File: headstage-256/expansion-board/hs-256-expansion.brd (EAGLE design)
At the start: 34 x 28.2 mm, 16 parts, among them J2 PINHD-2X5_DF40-REC, J4 PINHD-2X5_DF40-REC, J5 PINHD-2X6, J6 PINHD-2X4

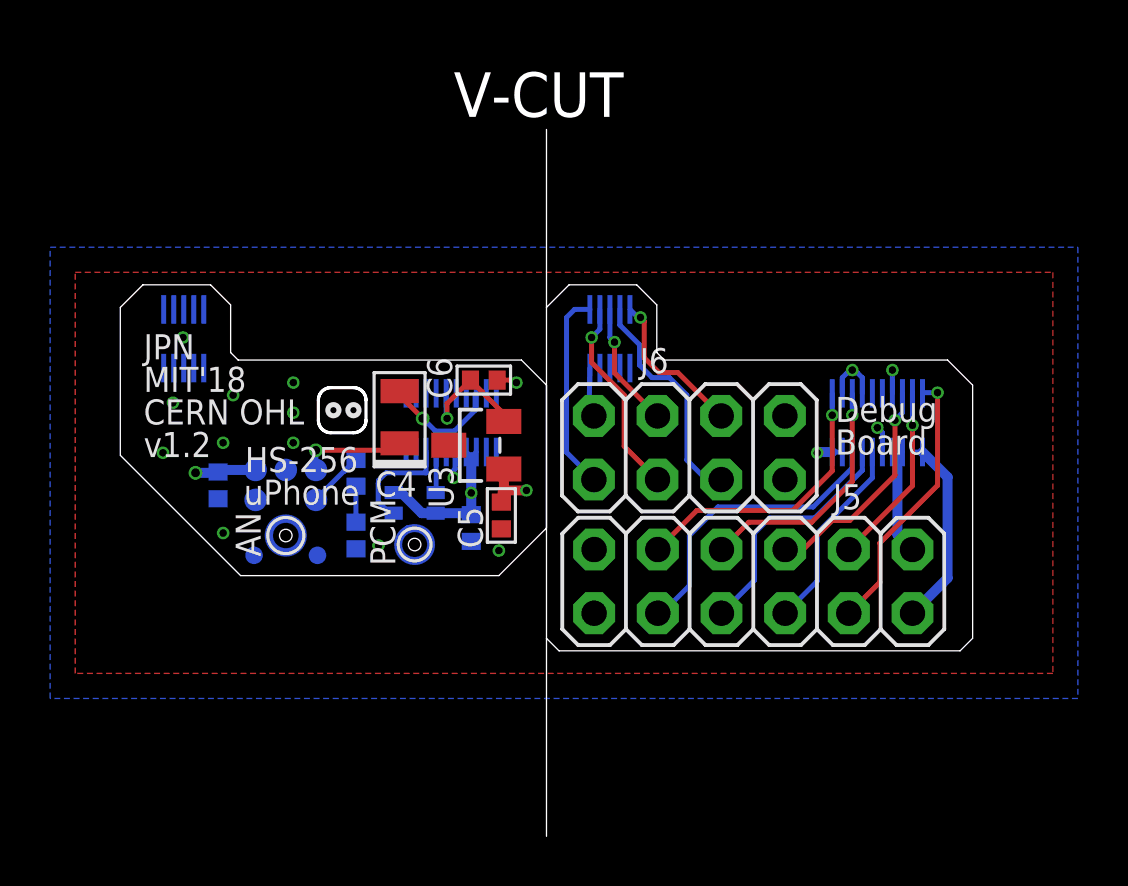
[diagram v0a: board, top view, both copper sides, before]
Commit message: Fix errors in headstage-256 expansion boards
- Headers were too close to receptacles in debug board
- Some components did not have values
- Added BOM to the google sheet based on this design
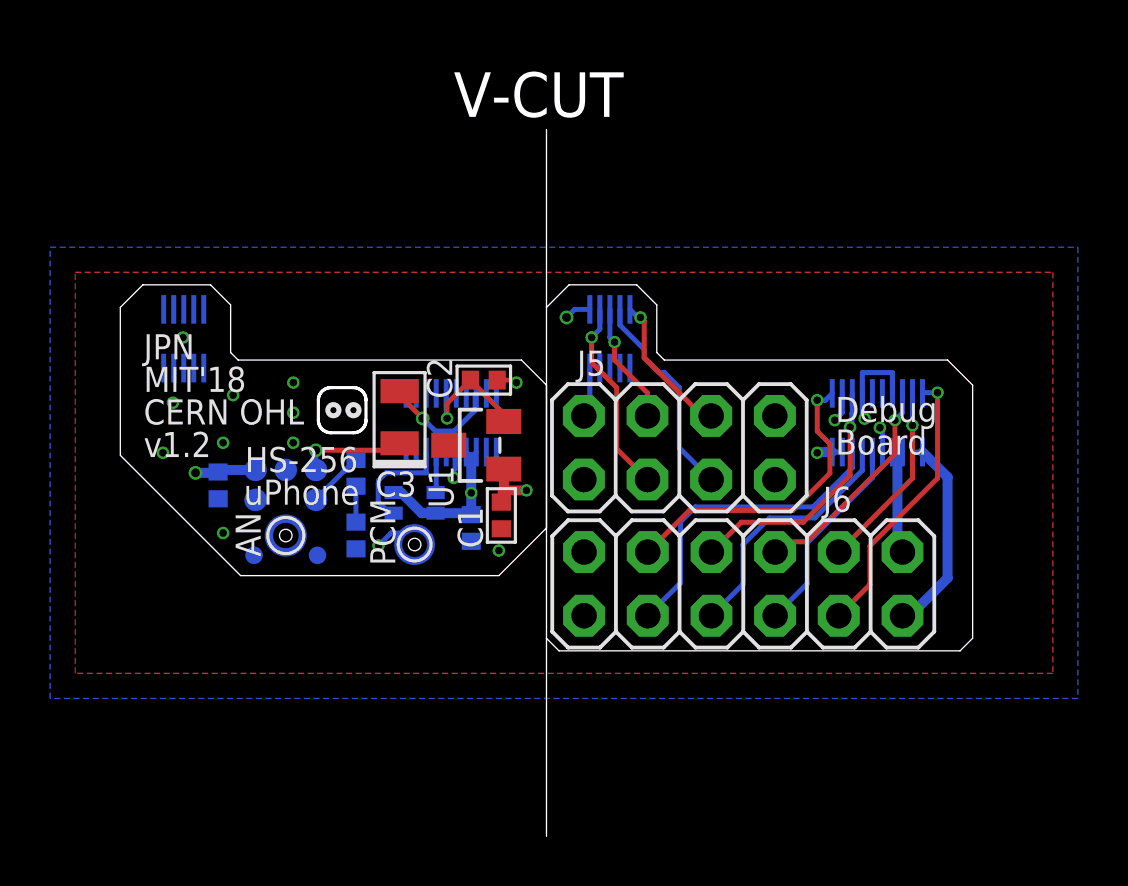
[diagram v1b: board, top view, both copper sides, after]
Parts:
- C3: value 1uF -> 10uF; device jonnew:0402 -> jonnew:0805-POL
- C4: value (none) -> 0.1uF; device jonnew:0805-POL -> jonnew:0402
- C5: value (none) -> 0.1uF
- C6: value 0.1uF -> 1uF
- J3: value (none) -> PINHD-2X5_DF40-REC; device jonnew:DF40-20REC -> jonnew:DF40-10REC
- J4: value PINHD-2X5_DF40-REC -> (none); device jonnew:DF40-10REC -> jonnew:DF40-20REC
- J5: value PINHD-2X6 -> PINHD-2X4; device jonnew:2X06-BIG -> jonnew:2X04-BIG
- J6: value PINHD-2X4 -> PINHD-2X6; device jonnew:2X04-BIG -> jonnew:2X06-BIG
- U1: value (none) -> REF3318; device jonnew:KNOWLES-SPH -> jonnew:SOT23
- U2: value (none) -> SPM0408LE5H-TB-6
- U3: value (none) -> SPH0641LU4H-1; device jonnew:SOT23 -> jonnew:KNOWLES-SPH
- moved C2 11.4 mm to (1.30, 1.70), flipped to the top, turned to 0 degrees
- moved C5 11.4 mm to (-9.30, -2.50), flipped to the bottom
- moved J3 11.2 mm to (6.33, 3.35)
- moved J4 11.2 mm to (17.0, 0.00)
- moved C6 8.03 mm to (-3.80, -4.50), flipped to the bottom, turned to 270 degrees
- moved J6 7.91 mm to (5.30, -7.70)
- moved J5 7.42 mm to (9.10, -1.00)
- moved C4 5.26 mm to (0.80, -4.20), flipped to the bottom, turned to 270 degrees
- moved C3 5.03 mm to (-2.06, 0.22), flipped to the top, turned to 90 degrees
- moved U1 4.66 mm to (1.00, -0.90), flipped to the top, turned to 90 degrees
- moved U3 4.66 mm to (-1.46, -4.86), flipped to the bottom, turned to 0 degrees
- moved C1 1.30 mm to (2.00, -3.70), flipped to the top
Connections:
- net +3V3: now also C4.1, J3.7, J3.8, J4.17, J4.18, J6.12, U1.1, U3.2, U3.5; no longer C2.1, J3.17, J3.18, J4.7, J4.8, J5.12, U1.2, U1.5, U3.1
- net A/D_IN1: now also J4.5; no longer J3.5
- net A/D_VREF: now also J4.6; no longer J3.6
- net ANOUT: now also C3.C; no longer C4.C
- net CLK: now also U3.4; no longer U1.4
- net DATA: now also U3.1; no longer U1.1
- net EXP1: now also J4.13, J6.3; no longer J3.13, J5.3
- net EXP10: now also J3.4, J5.3; no longer J4.4, J6.3
- net EXP11: now also J3.2, J5.5; no longer J4.2, J6.5
- net EXP12: now also J3.1, J5.6; no longer J4.1, J6.6
- net EXP13: now also J3.3, J5.4; no longer J4.3, J6.4
- net EXP14: now also J3.6, J5.2; no longer J4.6, J6.2
- net EXP2: now also J4.2, J6.10; no longer J3.2, J5.10
- net EXP3: now also J4.8, J6.6; no longer J3.8, J5.6
- net EXP4: now also J4.10, J6.4; no longer J3.10, J5.4
- net EXP5/VMEAS: now also J4.1, J6.9; no longer J3.1, J5.9
- net EXP6: now also J4.14, J6.5; no longer J3.14, J5.5
- net EXP7: now also J4.3, J6.8; no longer J3.3, J5.8
- net EXP8: now also J4.15, J6.7; no longer J3.15, J5.7
- net EXP9: now also J3.5, J5.1; no longer J4.5, J6.1
- net GND: now also C4.2, J3.10, J4.11, J4.12, J4.16, J4.4, J4.7, J5.7, J5.8, J6.1, J6.2, U3.6; no longer C3.2, J3.11, J3.12, J3.16, J3.4, J3.7, J4.10, J5.1, J5.2, J6.7, J6.8, U1.6
- net N$1: now also C6.1; no longer C3.1
- net N$5: now also C3.A; no longer C4.A
- net VCOAX: now also J4.19, J4.20, J6.11; no longer J3.19, J3.20, J5.11
- net VREF: now also C2.1, U1.2; no longer C6.1, U3.2
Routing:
- net GND: track 7.44 -> 10.7 mm
- net EXP9: track 7.98 -> 9.46 mm, vias 0 -> 1
- net EXP4: track 11.4 -> 12.4 mm
- net EXP11: track 9.21 -> 8.42 mm
- net EXP1: track 12.0 -> 12.7 mm

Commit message: Replaced v-cut with tabs on headstage-256 expansion boards
- Fab was unable to do a v-cut on a board this small
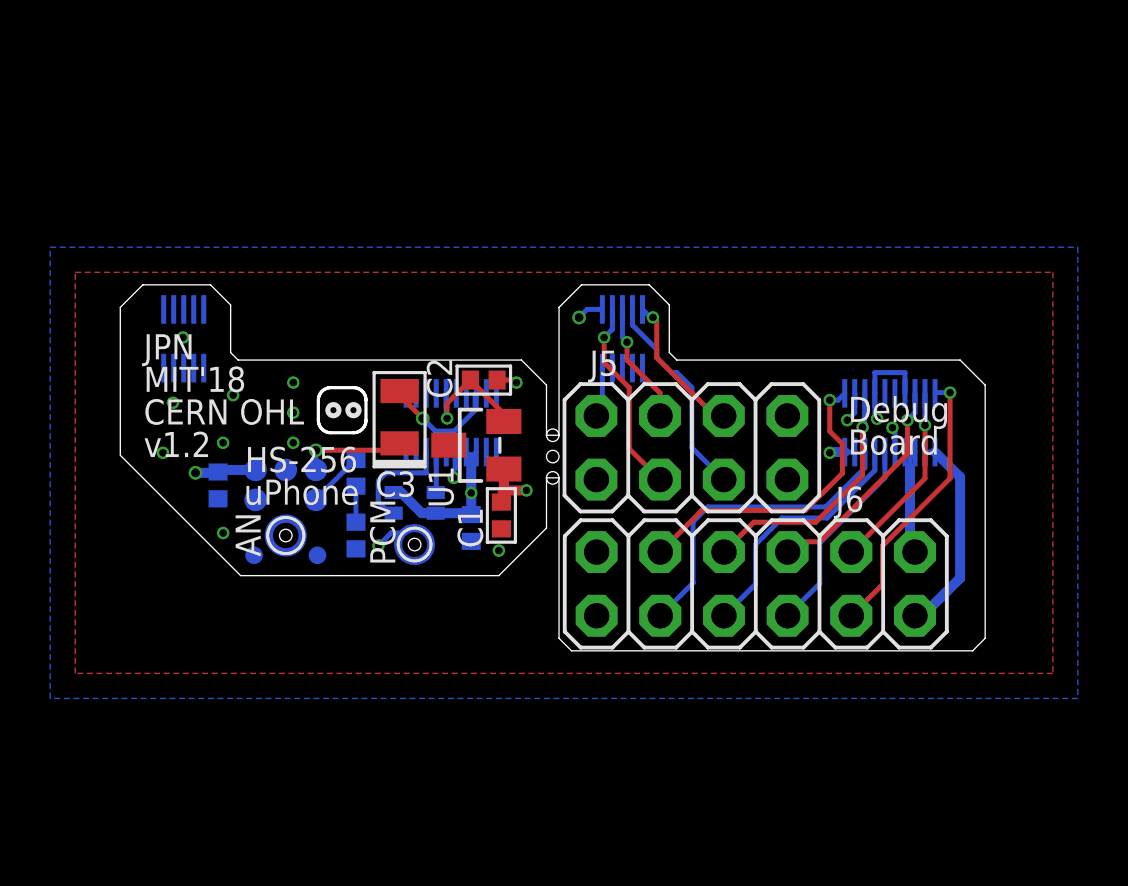
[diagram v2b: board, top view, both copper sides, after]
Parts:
- moved J3 0.50 mm to (6.83, 3.35)
- moved J4 0.50 mm to (17.5, 0.00)
- moved J5 0.50 mm to (9.60, -1.00)
- moved J6 0.50 mm to (5.80, -7.70)
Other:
- board size 34 x 28.2 mm -> 34.5 x 14.6 mm
- board text removed: "V-CUT"

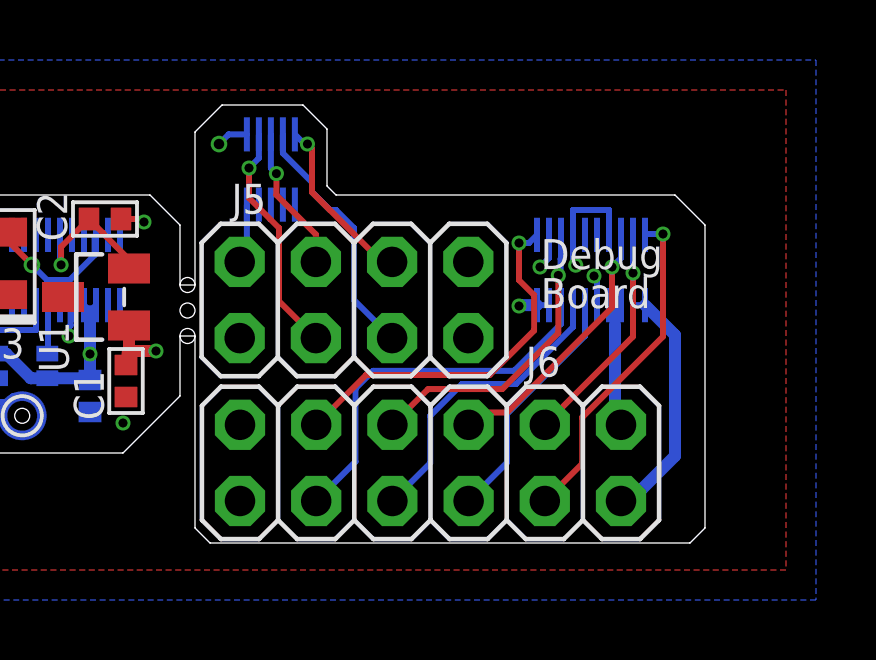
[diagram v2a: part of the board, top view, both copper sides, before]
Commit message: Widened mouse bites on hs-256 expansion boards
- To meet seeed DRC requirements
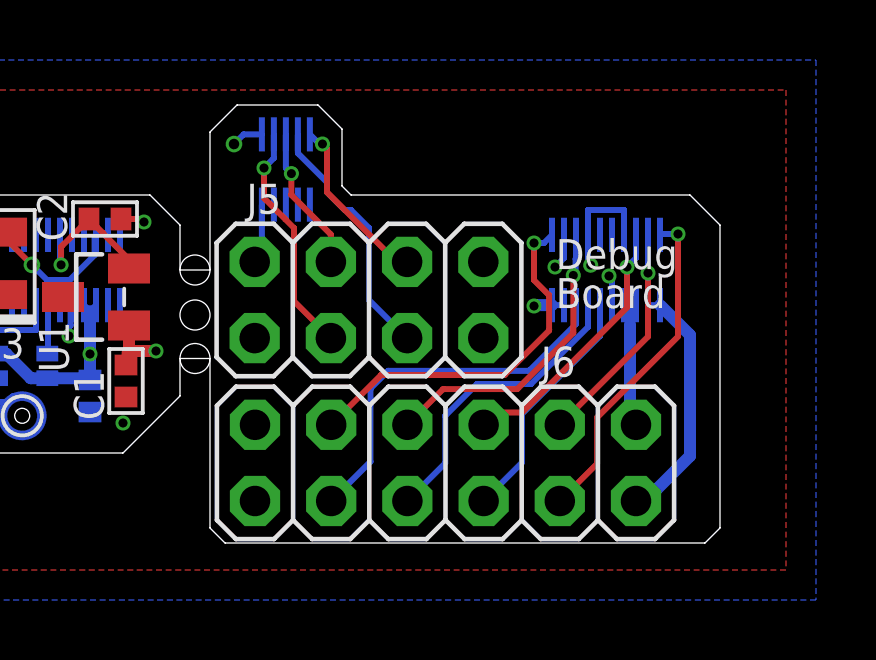
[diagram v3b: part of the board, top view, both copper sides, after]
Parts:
- moved J3 0.50 mm to (7.33, 3.35)
- moved J4 0.50 mm to (18.0, 0.00)
- moved J5 0.50 mm to (10.1, -1.00)
- moved J6 0.50 mm to (6.30, -7.70)
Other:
- board size 34.5 x 14.6 mm -> 35 x 14.6 mm
